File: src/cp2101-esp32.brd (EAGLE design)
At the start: 54 x 85.6 mm, 4 parts

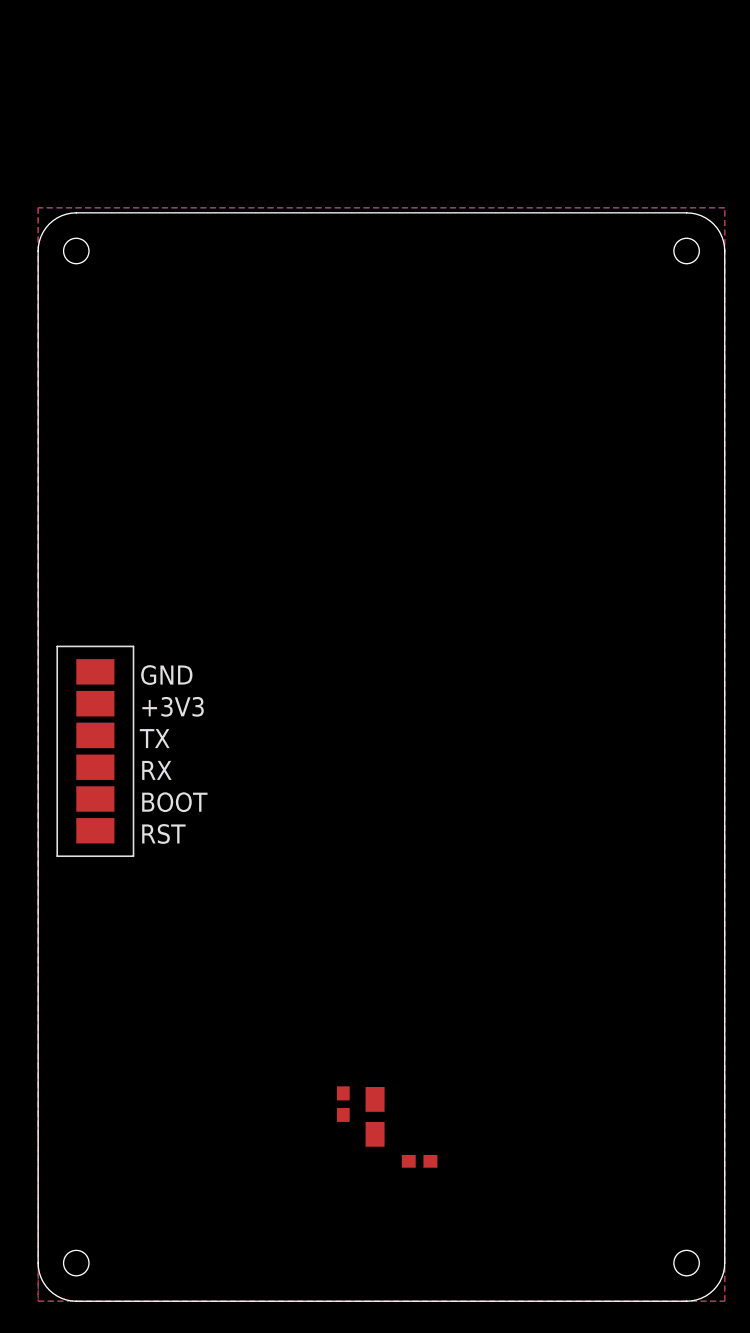
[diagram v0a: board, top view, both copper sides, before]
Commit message: Added connectors
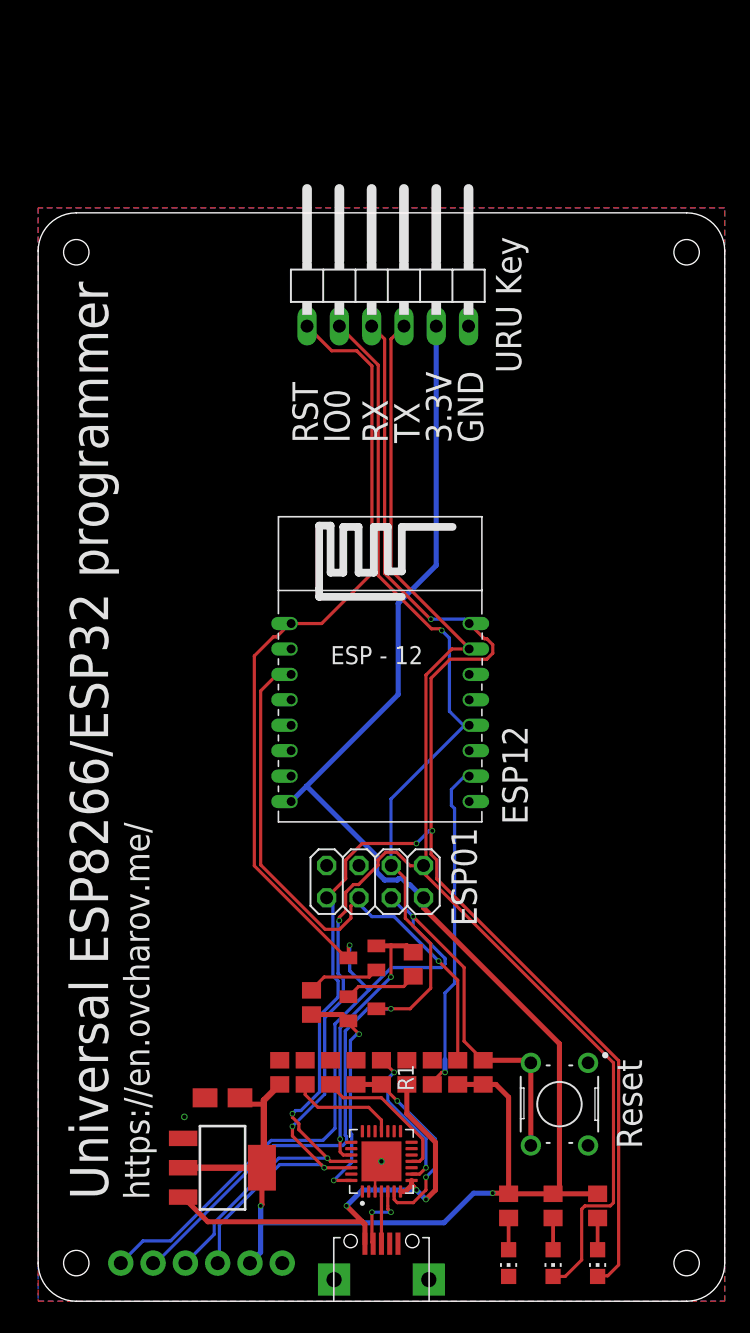
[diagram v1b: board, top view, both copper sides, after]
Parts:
- removed U$15: PROG, pads:PADS-6
- added C1, C3: 10u, rcl:C0805
- added IC1: LM1117MPX-3.3, lm1117:SOT223
- added JP1: URU_KEY, pinhead:1X06/90
- added JP2: ESP01, pinhead:2X04
- added LED1: POWER, led:CHIP-LED0805
- added LED2: TXD, led:CHIP-LED0805
- added LED3: RXD, led:CHIP-LED0805
- added R1, R7: 4.7K, rcl:R0805
- added R10, R2, R3, R8, R9: 10K, rcl:R0805
- added R4, R5, R6: 680, rcl:R0805
- added S1: B3F-1000, B3F-1000:SW_B3F-1000
- added T1, T2: BC847, transistor:SOT23
- added U$1: MICRO-USB, microusb:MICRO-USB
- added U$2: CONNPINS, CONN:PINS
- added U1: CP2102-GM, CP2102-GM:QFN50P500X500X100-29N
- added U2: ESP12, esp8266modules:ESP12
- C10, C8: device rcl:C0603 -> rcl:C0805
- moved C2 12.1 mm to (14.5, 16.0), turned to 0 degrees
- moved C10 7.07 mm to (29.0, 18.0), turned to 90 degrees
- moved C8 5.59 mm to (19.0, 18.0), turned to 90 degrees
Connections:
- new net CH_PD: JP2.3, R9.1, U2.CH_PD
- new net D+: U$1.3, U1.4
- new net D-: U$1.2, U1.5
- new net DTR: R2.1, T2.2, U1.28
- new net GPIO2: JP2.4
- new net N$1: C1.1, U1.18
- new net N$10: LED2.A, R5.1
- new net N$11: LED3.A, R6.1
- new net N$2: C3.1, R1.2, U1.6
- new net N$3: R7.2, U1.11
- new net N$4: R8.2, U2.GPIO15
- new net N$6: LED1.A, R4.1
- new net N$7: R1.1, U1.9
- new net N$8: R2.2, T1.1
- new net N$9: R3.2, T2.1
- new net RTS: R3.1, T1.2, U1.24
- net +3V3: now also IC1.2, IC1.TAB, JP1.5, JP2.7, R10.2, R4.2, R5.2, R6.2, R9.2, U$2.P$5, U2.VCC; no longer U$15.P5
- net GND: now also C1.2, C3.2, IC1.1, JP1.6, JP2.2, LED1.C, R7.1, R8.1, S1.1, S1.2, U$1.5, U$1.GND1, U$1.GND2, U$2.P$6, U1.29, U1.3, U2.GND; no longer U$15.P6
- net IO0: now also JP1.2, JP2.6, T2.3, U$2.P$2, U2.GPIO0; no longer U$15.P2
- net RST: now also JP1.1, JP2.5, R10.1, S1.3, S1.4, T1.3, U$2.P$1, U2.RESET; no longer U$15.P1
- net RXD: now also JP1.3, JP2.1, LED3.C, U$2.P$3, U1.25, U2.TX; no longer U$15.P3
- net TXD: now also JP1.4, JP2.8, LED2.C, U$2.P$4, U1.26, U2.RX; no longer U$15.P4
- net VBUS: now also IC1.3, U$1.1, U1.7, U1.8
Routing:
- net +3V3: track 0.00 -> 147.9 mm, vias 0 -> 2
- net RXD: track 0.00 -> 143.6 mm, vias 0 -> 5
- net TXD: track 0.00 -> 138.3 mm, vias 0 -> 3
- net RST: track 0.00 -> 137.9 mm, vias 0 -> 2
- net IO0: track 0.00 -> 97.8 mm, vias 0 -> 2
- net CH_PD: track 0.00 -> 45.1 mm, vias 0 -> 1
- net VBUS: track 0.00 -> 37.8 mm, vias 0 -> 3
- net N$4: track 0.00 -> 26.2 mm, vias 0 -> 1
- net RTS: track 0.00 -> 21.9 mm, vias 0 -> 2
- net DTR: track 0.00 -> 18.4 mm, vias 0 -> 2
- net N$2: track 0.00 -> 16.0 mm, vias 0 -> 2
- net N$7: track 0.00 -> 11.8 mm, vias 0 -> 2
- net N$3: track 0.00 -> 11.5 mm
- net N$1: track 0.00 -> 8.51 mm
- net N$9: track 0.00 -> 5.79 mm
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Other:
- board text added: "3.3V"
- board text added: "ESP01"
- board text added: "ESP12"
- board text added: "IO0"
- board text added: "Reset"
- board text added: "URU Key"
- board text added: "Universal ESP8266/ESP32 programmer"
- board text added: "https://en.ovcharov.me/"
- board text removed: "+3V3"
- board text removed: "BOOT"

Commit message: v1
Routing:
- net RXD: track 143.6 -> 141.6 mm
- net TXD: track 138.3 -> 137.6 mm
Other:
- board text removed: "URU Key"
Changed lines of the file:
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@@
 <text x="34.5" y="29.5" size="2" layer="25" font="vector" rot="R90">ESP01</text>
 <text x="47.5" y="12" size="2" layer="25" font="vector" rot="R90">Reset</text>
-<text x="38" y="73" size="2" layer="25" font="vector" rot="R90">URU Key</text>
 <text x="22" y="67.5" size="2" layer="25" font="vector" rot="R90">RST</text>
 <text x="24.5" y="67.5" size="2" layer="25" font="vector" rot="R90">IO0</text>
@@
 <wire x1="14.25" y1="3" x2="14.12" y2="3" width="0.25" layer="16"/>
 <via x="22.5" y="10.5" extent="1-16" drill="0.3"/>
-<wire x1="22.5" y1="10.5" x2="20" y2="13" width="0.254" layer="1"/>
-<wire x1="20" y1="13" x2="20" y2="13.75" width="0.254" layer="1"/>
-<via x="20" y="13.75" extent="1-16" drill="0.3"/>
-<wire x1="20" y1="13.75" x2="22.5328" y2="16.2828" width="0.254" layer="16"/>
 <wire x1="22.5328" y1="16.2828" x2="22.5328" y2="22.2828" width="0.254" layer="16"/>
 <wire x1="22.5328" y1="22.2828" x2="24" y2="23.75" width="0.254" layer="16"/>
@@
 <wire x1="29.2627625" y1="34.25" x2="30.29" y2="34.25" width="0.254" layer="1"/>
 <wire x1="30.29" y1="34.25" x2="30.31" y2="34.27" width="0.254" layer="1"/>
+<via x="21.7101" y="14" extent="1-16" drill="0.35"/>
+<wire x1="22.5" y1="10.5" x2="22.5" y2="10.7878" width="0.25" layer="1"/>
+<wire x1="21.8476" y1="13.8625" x2="21.7101" y2="14" width="0.25" layer="1"/>
+<wire x1="22.5" y1="10.7878" x2="21.8476" y2="11.4402" width="0.25" layer="1"/>
+<wire x1="21.8476" y1="11.4402" x2="21.8476" y2="13.8625" width="0.25" layer="1"/>
+<wire x1="22.0263625" y1="13.9601" x2="22.4736375" y2="13.9601" width="0.25" layer="16"/>
+<wire x1="22.4736375" y1="13.9601" x2="22.7899" y2="14.2763625" width="0.25" layer="16"/>
+<wire x1="22.7899" y1="14.2763625" x2="22.7899" y2="14.7236375" width="0.25" layer="16"/>
+<wire x1="22.7899" y1="14.7236375" x2="22.5328" y2="14.9807375" width="0.25" layer="16"/>
+<wire x1="22.5328" y1="14.9807375" x2="22.5328" y2="16.2828" width="0.25" layer="16"/>
+<wire x1="21.7101" y1="14" x2="21.9864625" y2="14" width="0.25" layer="16"/>
+<wire x1="21.9864625" y1="14" x2="22.0263625" y2="13.9601" width="0.25" layer="16"/>
 </signal>
 <signal name="RXD">
@@
 <via x="31.0036" y="37" extent="1-16" drill="0.3"/>
 <wire x1="31.0036" y1="37" x2="30.9044" y2="37" width="0.254" layer="1"/>
-<via x="20" y="14.75" extent="1-16" drill="0.3"/>
-<wire x1="22.75" y1="11.25" x2="20.5056" y2="13.4944" width="0.254" layer="1"/>
-<wire x1="20" y1="14.46503125" x2="20" y2="14.75" width="0.254" layer="1"/>
-<wire x1="20.5056" y1="13.4944" x2="20.5056" y2="13.95943125" width="0.254" layer="1"/>
-<wire x1="20.5056" y1="13.95943125" x2="20" y2="14.46503125" width="0.254" layer="1"/>
-<wire x1="20" y1="14.75" x2="20.25" y2="15" width="0.254" layer="16"/>
-<wire x1="20.25" y1="15" x2="20.6752625" y2="15" width="0.254" layer="16"/>
 <wire x1="22.1264" y1="16.4511375" x2="22.1264" y2="22.4511375" width="0.254" layer="16"/>
 <wire x1="22.1264" y1="22.4511375" x2="23.5936" y2="23.9183375" width="0.254" layer="16"/>
 <wire x1="23.5936" y1="25.1821875" x2="23.1816" y2="25.5941875" width="0.254" layer="16"/>
 <wire x1="23.1816" y1="31.2384" x2="22.69" y2="31.73" width="0.254" layer="16"/>
-<wire x1="20.6752625" y1="15" x2="22.1264" y2="16.4511375" width="0.254" layer="16"/>
 <wire x1="23.5936" y1="23.9183375" x2="23.5936" y2="25.1821875" width="0.254" layer="16"/>
 <wire x1="23.1816" y1="25.5941875" x2="23.1816" y2="31.2384" width="0.254" layer="16"/>
+<wire x1="22.75" y1="11.25" x2="22.25" y2="11.75" width="0.25" layer="1"/>
+<wire x1="22.25" y1="11.75" x2="22.25" y2="14.5" width="0.25" layer="1"/>
+<via x="22.25" y="14.5" extent="1-16" drill="0.35"/>
+<wire x1="22.25" y1="14.5" x2="22.1264" y2="14.6236" width="0.25" layer="16"/>
+<wire x1="22.1264" y1="14.6236" x2="22.1264" y2="16.4511375" width="0.25" layer="16"/>
 </signal>
 <signal name="RST">
@@
 <wire x1="6.5" y1="3" x2="8.25" y2="4.75" width="0.254" layer="16"/>
 <wire x1="10.4252625" y1="4.75" x2="18.3260625" y2="12.6508" width="0.254" layer="16"/>
-<wire x1="18.3260625" y1="12.6508" x2="22.4008" y2="12.6508" width="0.254" layer="16"/>
+<wire x1="18.3260625" y1="12.6508" x2="22.9008" y2="12.6508" width="0.254" layer="16"/>
 <wire x1="31.70943125" y1="26.2444" x2="32.0056" y2="26.54056875" width="0.254" layer="16"/>
 <wire x1="32.0056" y1="26.54056875" x2="32.0056" y2="26.95943125" width="0.254" layer="16"/>
 <wire x1="29.5" y1="29.46503125" x2="29.5" y2="30.25" width="0.254" layer="16"/>
 <wire x1="32.0056" y1="26.95943125" x2="29.5" y2="29.46503125" width="0.254" layer="16"/>
-<wire x1="23.3456" y1="13.5956" x2="23.3456" y2="21.81063125" width="0.254" layer="16"/>
+<wire x1="23.3456" y1="13.0956" x2="23.3456" y2="21.81063125" width="0.254" layer="16"/>
 <wire x1="23.3456" y1="21.81063125" x2="26.017484375" y2="24.482515625" width="0.254" layer="16"/>
 <wire x1="26.017484375" y1="24.482515625" x2="27.77936875" y2="26.2444" width="0.254" layer="16"/>
 <wire x1="27.77936875" y1="26.2444" x2="31.70943125" y2="26.2444" width="0.254" layer="16"/>
 <wire x1="8.25" y1="4.75" x2="10.4252625" y2="4.75" width="0.254" layer="16"/>
-<wire x1="22.4008" y1="12.6508" x2="23.3456" y2="13.5956" width="0.254" layer="16"/>
+<wire x1="22.9008" y1="12.6508" x2="23.3456" y2="13.0956" width="0.254" layer="16"/>
 <wire x1="24.4" y1="27" x2="24.4" y2="27.9" width="0.254" layer="1"/>
 <wire x1="24.4" y1="27.9" x2="24.5" y2="28" width="0.254" layer="1"/>

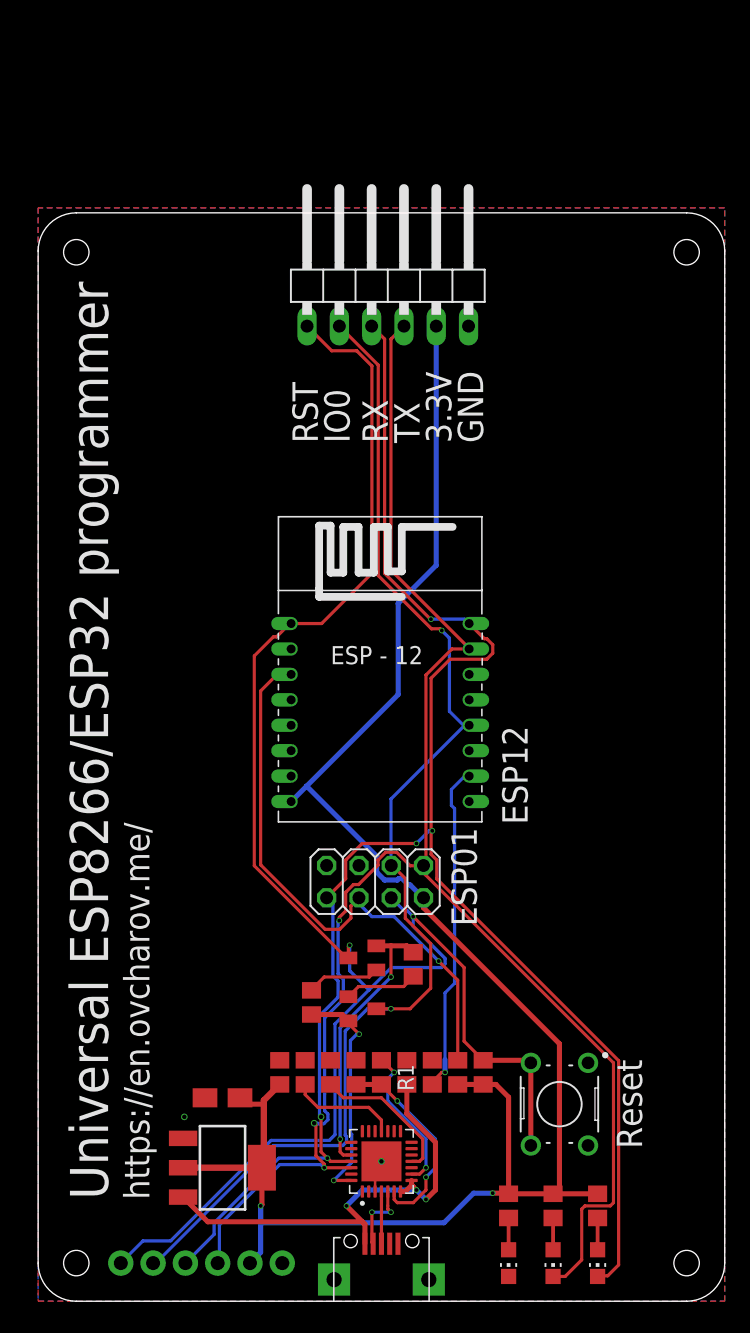
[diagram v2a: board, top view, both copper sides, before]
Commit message: USB TypeC connector; Smaller board
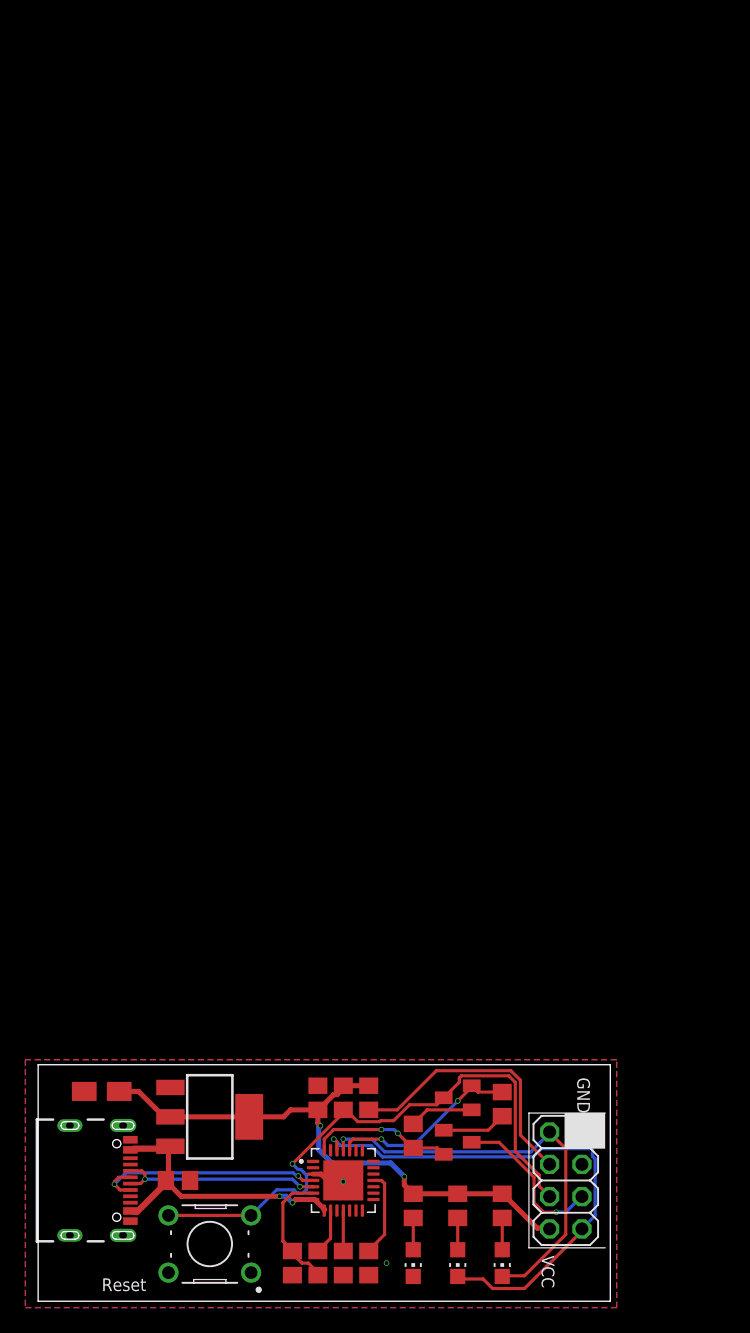
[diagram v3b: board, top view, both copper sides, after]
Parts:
- removed JP1: URU_KEY, pinhead:1X06/90
- removed R8: 10K, rcl:R0805
- removed U$1: MICRO-USB, microusb:MICRO-USB
- removed U$2: CONNPINS, CONN:PINS
- removed U2: ESP12, esp8266modules:ESP12
- added J1: USB4105_REVA, USB4105_REVA:GCT_USB4105_REVA
- moved S1 29.6 mm to (13.5, 4.50), turned to 180 degrees
- moved JP2 27.9 mm to (41.5, 9.50), turned to 270 degrees
- moved C10 19.9 mm to (11.0, 9.50), turned to 0 degrees
- moved C1 15.8 mm to (26.0, 3.00), turned to 270 degrees
- moved C3 15.8 mm to (20.0, 3.00), turned to 270 degrees
- moved R1 15.8 mm to (22.0, 3.00)
- moved R7 15.0 mm to (24.0, 3.00), turned to 90 degrees
- moved T1 13.3 mm to (33.0, 16.0)
- moved R2 13.2 mm to (29.5, 13.0)
- moved R3 13.0 mm to (36.5, 15.5)
- moved T2 12.9 mm to (33.0, 12.5)
- moved R10 11.2 mm to (24.0, 16.0), turned to 90 degrees
- moved C2 9.51 mm to (5.00, 16.5)
- moved LED1 7.50 mm to (29.5, 3.00)
- moved LED2 7.50 mm to (33.0, 3.00)
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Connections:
- net N$2 renamed VDD
- net N$3 renamed !SUSPEND
- net N$7 renamed !RST
- removed net N$4: R8.2, U2.GPIO15
- net +3V3: no longer JP1.5, U$2.P$5, U2.VCC
- net CH_PD: no longer U2.CH_PD
- net D+: now also J1.A6, J1.B6; no longer U$1.3
- net D-: now also J1.A7, J1.B7; no longer U$1.2
- net GND: now also J1.A1/B12, J1.B1/A12, J1.G1, J1.G2, J1.G3, J1.G4; no longer JP1.6, R8.1, U$1.5, U$1.GND1, U$1.GND2, U$2.P$6, U2.GND
- net IO0: no longer JP1.2, U$2.P$2, U2.GPIO0
- net RST: no longer JP1.1, U$2.P$1, U2.RESET
- net RXD: no longer JP1.3, U$2.P$3, U2.TX
- net TXD: no longer JP1.4, U$2.P$4, U2.RX
- net VBUS: now also J1.A4/B9, J1.B4/A9; no longer U$1.1
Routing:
- net RXD: track 141.6 -> 33.2 mm, vias 5 -> 1
- net +3V3: track 147.9 -> 46.1 mm
- net TXD: track 137.6 -> 41.3 mm, vias 3 -> 1
- net RST: track 138.2 -> 46.3 mm, vias 2 -> 1
- net IO0: track 97.8 -> 12.6 mm, vias 2 -> 1
- net N$4: track 26.2 -> 0.00 mm, vias 1 -> 0
- net CH_PD: track 45.1 -> 21.1 mm, vias 1 -> 0
- net D+: track 4.11 -> 19.3 mm, vias 0 -> 2
- net VBUS: track 37.8 -> 23.7 mm, vias 3 -> 2
- net D-: track 5.75 -> 16.4 mm
- net !SUSPEND: track 11.5 -> 3.18 mm
- net !RST: track 11.8 -> 3.59 mm, vias 2 -> 0
- net DTR: track 18.4 -> 11.5 mm
- net RTS: track 21.9 -> 15.1 mm
- net VDD: track 16.0 -> 9.82 mm, vias 2 -> 0
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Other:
- board size 54 x 85.6 mm -> 45 x 18.6 mm
- board text added: "VCC"
- board text removed: "3.3V"
- board text removed: "ESP01"
- board text removed: "ESP12"
- board text removed: "IO0"
- board text removed: "RST"
- board text removed: "RX"
- board text removed: "TX"
- board text removed: "Universal ESP8266/ESP32 programmer"
- board text removed: "https://en.ovcharov.me/"

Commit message: .
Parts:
- removed C3: 10u, rcl:C0805
- removed R1, R7: 4.7K, rcl:R0805
- removed S1: B3F-1000, B3F-1000:SW_B3F-1000
- added R8: 10K, rcl:R0805
- added U$1: SWITCH2X4-MICRO, SMD Tact:2X4-MICRO
- U1: value CP2102-GM -> CP2104-F03-GM; device CP2102-GM:QFN50P500X500X100-29N -> CP2104:QFN50P400X400X80-25N
- moved LED1 26.5 mm to (3.00, 2.50), turned to 90 degrees
- moved R4 22.6 mm to (7.50, 2.50), turned to 0 degrees
- moved LED2 17.7 mm to (21.0, 16.0)
- moved C8 17.1 mm to (11.5, 2.50)
- moved LED3 16.1 mm to (27.0, 16.0)
- moved R9 13.8 mm to (29.0, 2.50), turned to 270 degrees
- moved R10 13.7 mm to (26.5, 2.50), turned to 270 degrees
- moved R5 13.1 mm to (23.0, 16.0)
- moved R3 12.6 mm to (24.5, 11.5), turned to 0 degrees
- moved T1 11.7 mm to (24.5, 8.00), turned to 180 degrees
- moved R6 11.3 mm to (29.0, 16.0)
- moved C1 9.51 mm to (16.5, 2.50)
- moved JP2 7.50 mm to (34.0, 9.50)
- moved R2 6.08 mm to (28.5, 7.00), turned to 180 degrees
- moved U1 5.10 mm to (19.0, 8.50)
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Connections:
- removed net !RST: R1.1, U1.9
- removed net !SUSPEND: R7.2, U1.11
- removed net VDD: C3.1, R1.2, U1.6
- new net N$7: C1.1, U1.16
- net +3V3: now also R8.2, U1.5, U1.6, U1.7
- net D+: now also U1.3; no longer U1.4
- net D-: now also U1.4; no longer U1.5
- net DTR: now also U1.23; no longer U1.28
- net GND: now also U$1.P$5, U1.2, U1.25; no longer C3.2, R7.1, S1.1, S1.2, U1.29, U1.3
- net N$1: now also R8.1, U1.9; no longer C1.1, U1.18
- net RST: now also U$1.P$4; no longer S1.3, S1.4
- net RTS: now also U1.19; no longer U1.24
- net RXD: now also U1.20; no longer U1.25
- net TXD: now also U1.21; no longer U1.26
- net VBUS: no longer U1.7, U1.8
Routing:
- net +3V3: track 46.1 -> 85.3 mm
- net RST: track 46.3 -> 15.9 mm, vias 1 -> 0
- net TXD: track 41.3 -> 22.8 mm
- net RXD: track 33.2 -> 17.0 mm, vias 1 -> 0
- net VBUS: track 23.7 -> 12.8 mm
- net CH_PD: track 21.1 -> 10.3 mm
- net N$7: track 0.00 -> 10.1 mm
- net VDD: track 9.82 -> 0.00 mm
- net RTS: track 15.1 -> 6.60 mm, vias 2 -> 0
- net D+: track 19.3 -> 13.3 mm, vias 2 -> 0
- net DTR: track 11.5 -> 16.2 mm
- net !RST: track 3.59 -> 0.00 mm
- net IO0: track 12.6 -> 9.20 mm, vias 1 -> 0
- net !SUSPEND: track 3.18 -> 0.00 mm
- net D-: track 16.4 -> 13.6 mm
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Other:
- board size 45 x 18.6 mm -> 38 x 18.6 mm
- board text added: "3.3V"
- board text added: "CH_PD"
- board text added: "ESP01"
- board text added: "IO0"
- board text added: "IO2"
- board text added: "RST"
- board text added: "RXD"
- board text added: "TXD"
- board text added: "USB - UART"
- board text added: "https://ovcharov.me"
- board text removed: "VCC"
